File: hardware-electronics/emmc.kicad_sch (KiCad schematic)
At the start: 29 parts, among them U2 EMMC16G-MW28-01E10, U4 24AA04T-I_OT, U8 USB2244-AEZG-06, Y2 ECS-240-10-47-CKM-TR

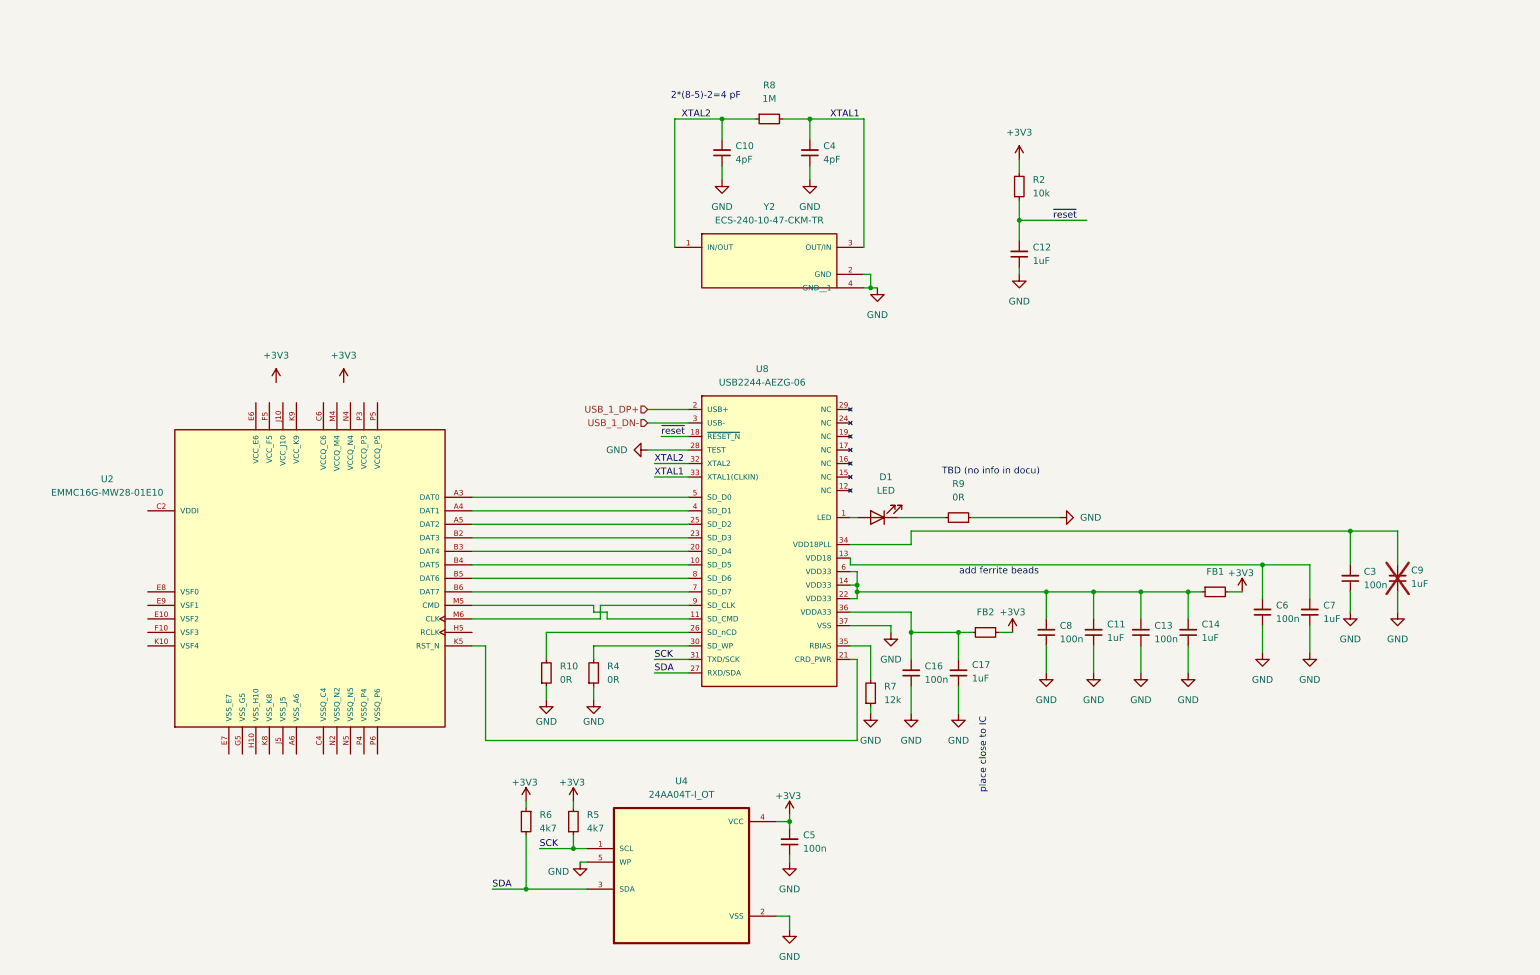
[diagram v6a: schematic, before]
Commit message: WIP SCH EMMC connect power to flash
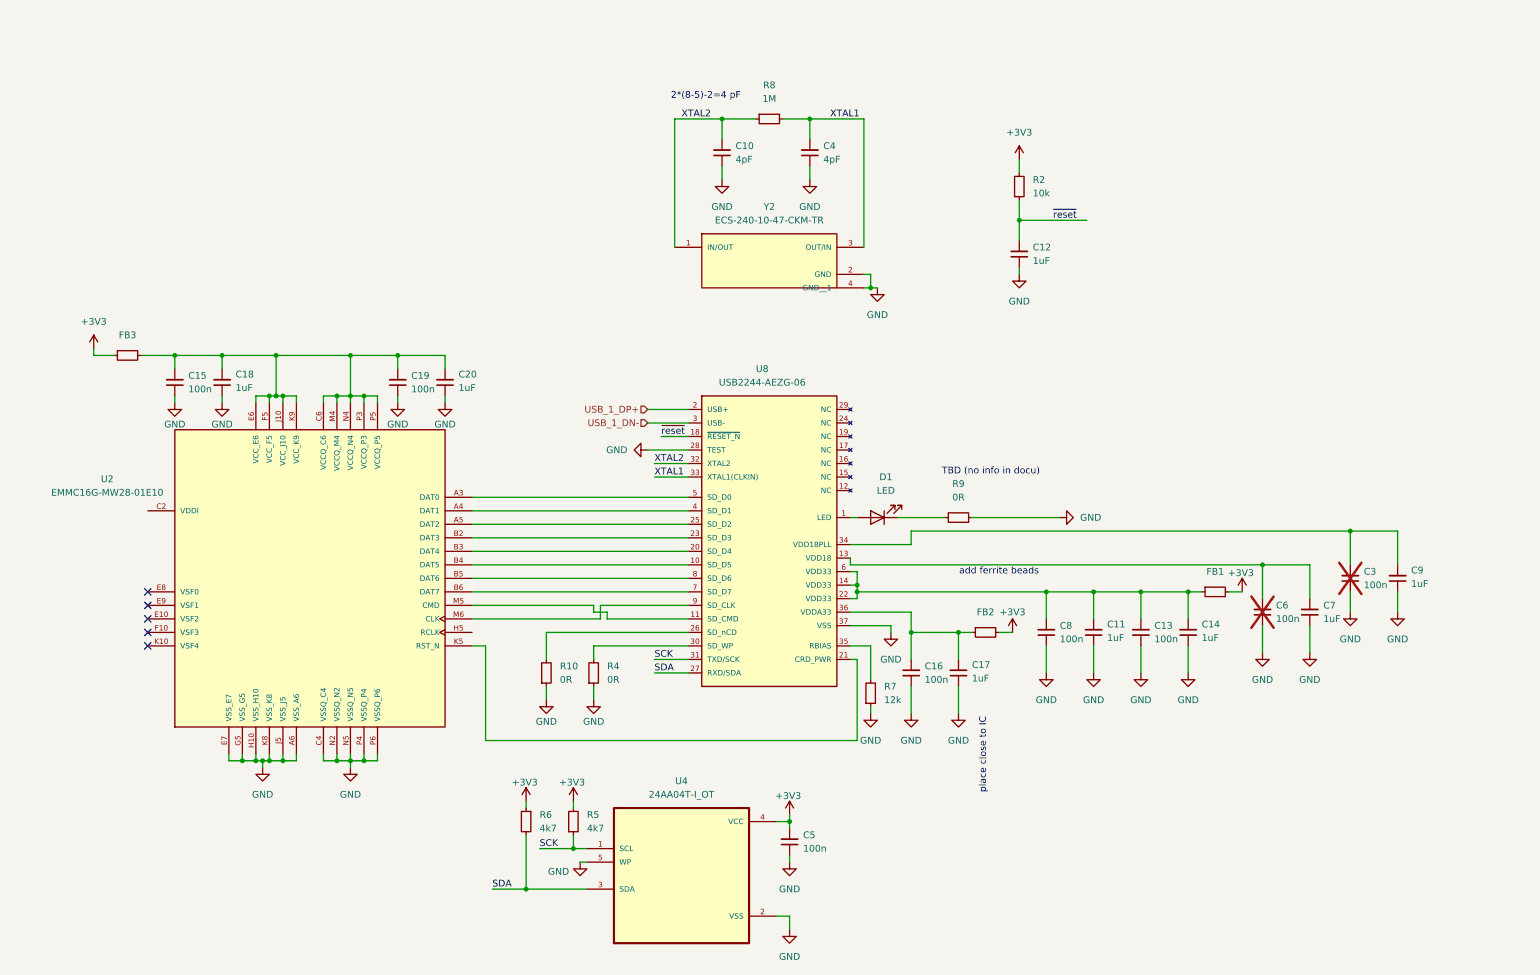
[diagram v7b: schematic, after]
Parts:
- added C15, C19: C_100n_0402, C_100n_0402:C_0402_1005Metric, symbol M2SmartHomeSymbols:C_100n_0402
- added C18, C20: C_1uF_0402, C_1uF_0402:C_0402_1005Metric, symbol M2SmartHomeSymbols:C_1uF_0402
- added FB3: FB_120R_0603, FB_120R_0603:FB_0603_1608Metric, symbol M2SmartHomeSymbols:FB_120R_0603
- C3, C6: now not fitted
- C9: now fitted
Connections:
- net +3V3: now also FB3.1
- net GND: now also U2.A6 (VSS_A6), U2.C4 (VSSQ_C4), U2.E7 (VSS_E7), U2.G5 (VSS_G5), U2.H10 (VSS_H10), U2.J5 (VSS_J5), U2.K8 (VSS_K8), U2.N2 (VSSQ_N2), U2.N5 (VSSQ_N5), U2.P4 (VSSQ_P4), U2.P6 (VSSQ_P6), C15.1, C18.1, C19.1, C20.1
- net at U2.C6 (VCCQ_C6): now also U2.E6 (VCC_E6), U2.F5 (VCC_F5), U2.J10 (VCC_J10), U2.K9 (VCC_K9), U2.M4 (VCCQ_M4), U2.N4 (VCCQ_N4), U2.P3 (VCCQ_P3), U2.P5 (VCCQ_P5), C15.2, C18.2, C19.2, C20.2, FB3.2
- no-connect marks 0 -> 5

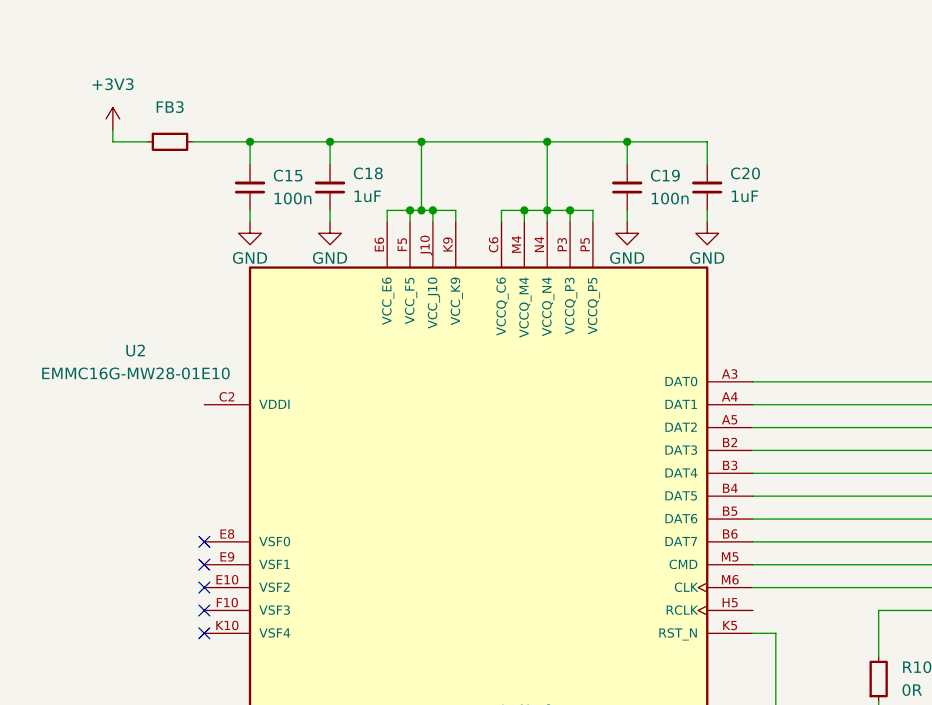
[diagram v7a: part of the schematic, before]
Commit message: #11 SCH EMMC flash add decoupling capacitors according to datasheet
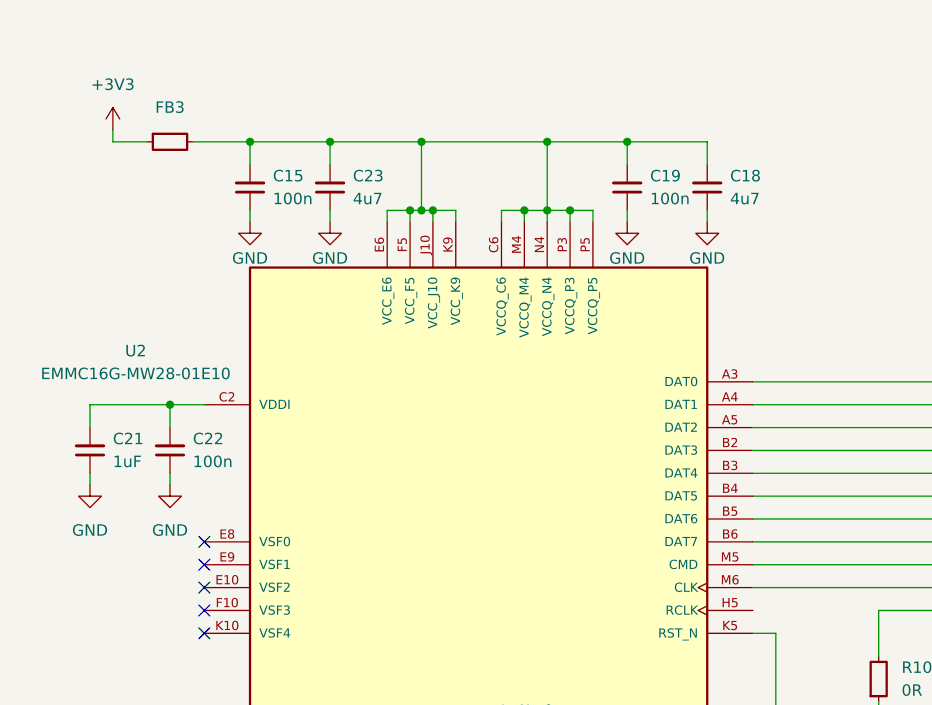
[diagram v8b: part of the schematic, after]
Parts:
- removed C18, C20: C_1uF_0402, C_1uF_0402:C_0402_1005Metric, symbol M2SmartHomeSymbols:C_1uF_0402
- added C18, C23: C_4u7_0402, C_4u7_0402:C_0402_1005Metric, symbol M2SmartHomeSymbols:C_4u7_0402
- added C21: C_1uF_0402, C_1uF_0402:C_0402_1005Metric, symbol M2SmartHomeSymbols:C_1uF_0402
- added C22: C_100n_0402, C_100n_0402:C_0402_1005Metric, symbol M2SmartHomeSymbols:C_100n_0402
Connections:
- net GND: now also C18.1, C21.1, C22.1, C23.1
- net at C15.2, C19.2, FB3.2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: now also C18.2, C23.2
- net at U2.C2 (VDDI): now also C21.2, C22.2
